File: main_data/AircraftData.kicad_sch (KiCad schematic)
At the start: 54 parts, among them J1 Orientation, J10 Shaft, J11 Wind Speed, J12 DHT, J13 RPi, J14 USB_C_Receptacle_USB2.0, J15 Control Board, J2 PROG, J3 SPI VIDEO, J4 Barometer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

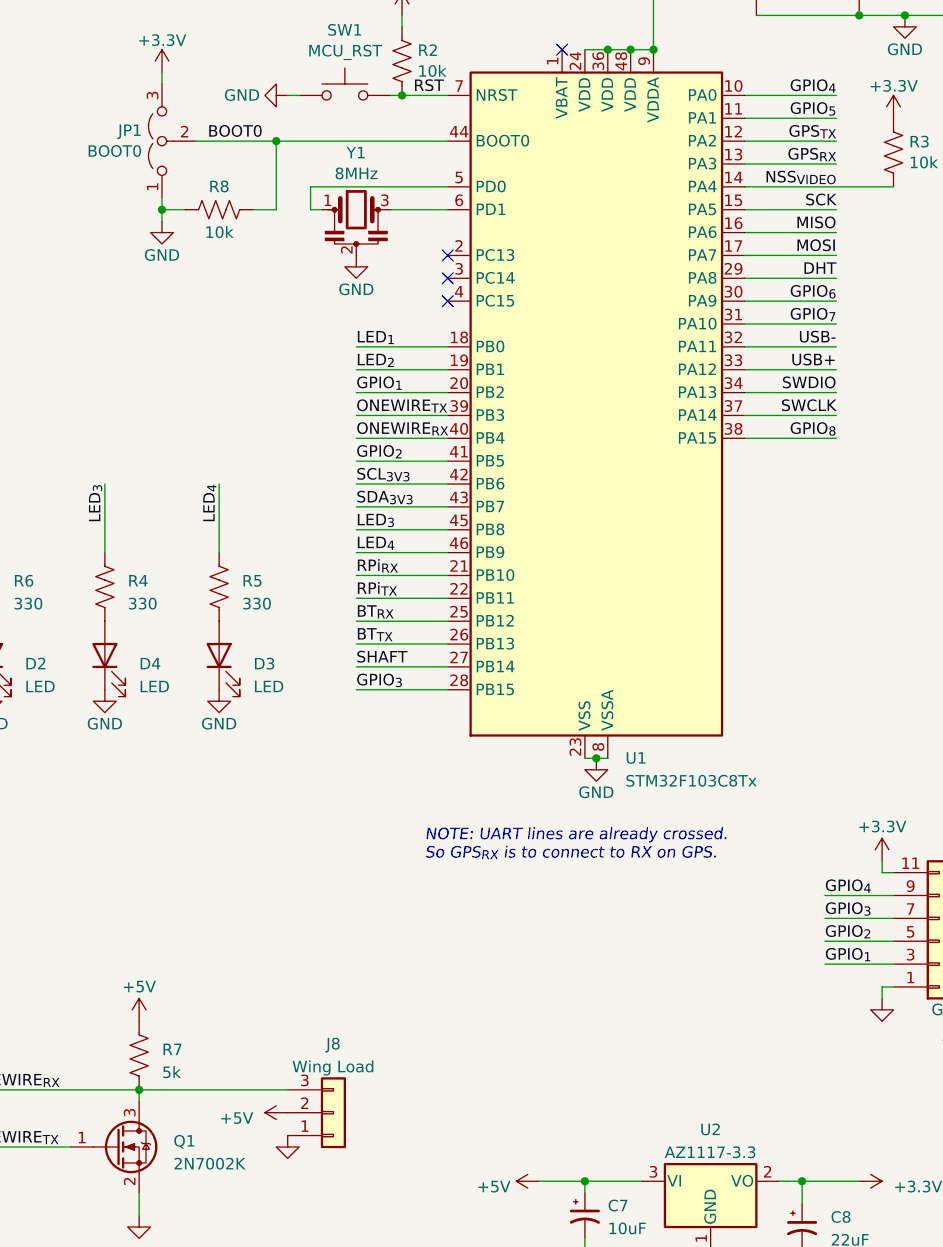
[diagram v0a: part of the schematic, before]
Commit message: Upgraded STM32
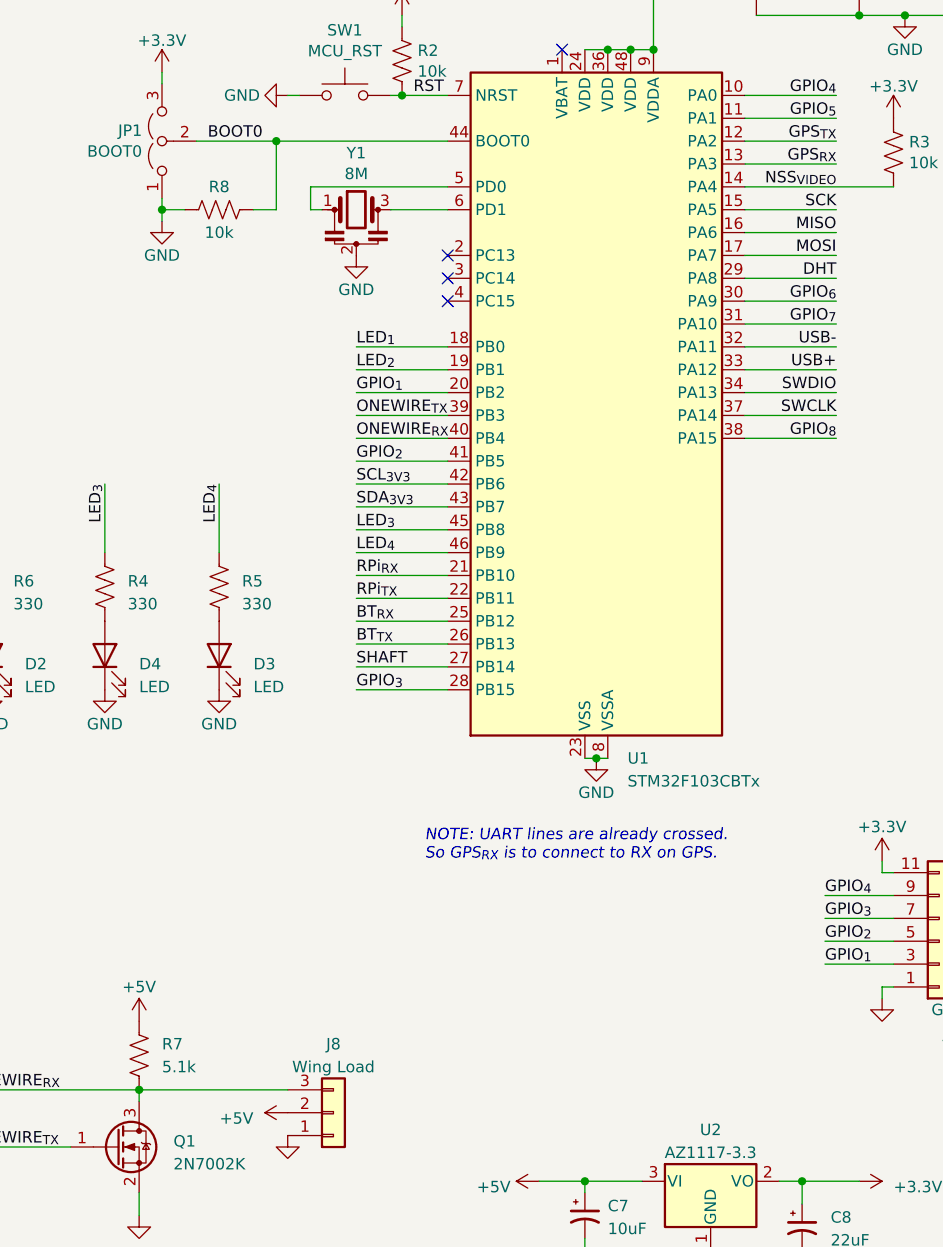
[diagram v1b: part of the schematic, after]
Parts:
- H1, H2, H3, JP1: now left out of the parts list
- R7: value 5k -> 5.1k
- U1: value STM32F103C8Tx -> STM32F103CBTx; symbol MCU_ST_STM32F1:STM32F103C8Tx -> MCU_ST_STM32F1:STM32F103CBTx
- Y1: value 8MHz -> 8M
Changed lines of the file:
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@@
   (symbol (lib_id "Device:R_US") (at 45.72 168.91 0) (unit 1)
     (in_bom yes) (on_board yes) (dnp no) (fields_autoplaced)
-    (property "Reference" "R7" (at 48.26 168.275 0)
-      (effects (font (size 1.27 1.27)) (justify left))
-    )
-    (property "Value" "5k" (at 48.26 170.815 0)
+    (property "Reference" "R7" (at 48.26 167.64 0)
+      (effects (font (size 1.27 1.27)) (justify left))
+    )
+    (property "Value" "5.1k" (at 48.26 170.18 0)
       (effects (font (size 1.27 1.27)) (justify left))
     )
@@
       (effects (font (size 1.27 1.27)))
     )
-    (property "Value" "8MHz" (at 69.85 70.9422 0)
+    (property "Value" "8M" (at 69.85 70.9422 0)
       (effects (font (size 1.27 1.27)))
     )
@@
   )
   (symbol (lib_id "Mechanical:MountingHole") (at 289.56 143.51 0) (unit 1)
-    (in_bom yes) (on_board yes) (dnp no) (fields_autoplaced)
+    (in_bom no) (on_board yes) (dnp no) (fields_autoplaced)
     (property "Reference" "H2" (at 292.1 142.875 0)
       (effects (font (size 1.27 1.27)) (justify left))
@@
     )
   )
-  (symbol (lib_id "MCU_ST_STM32F1:STM32F103C8Tx") (at 95.25 97.79 0) (unit 1)
-    (in_bom yes) (on_board yes) (dnp no) (fields_autoplaced)
-    (property "Reference" "U1" (at 99.7459 135.89 0)
-      (effects (font (size 1.27 1.27)) (justify left))
-    )
-    (property "Value" "STM32F103C8Tx" (at 99.7459 138.43 0)
+  (symbol (lib_id "MCU_ST_STM32F1:STM32F103CBTx") (at 95.25 97.79 0) (unit 1)
+    (in_bom yes) (on_board yes) (dnp no) (fields_autoplaced)
+    (property "Reference" "U1" (at 99.9841 135.89 0)
+      (effects (font (size 1.27 1.27)) (justify left))
+    )
+    (property "Value" "STM32F103CBTx" (at 99.9841 138.43 0)
       (effects (font (size 1.27 1.27)) (justify left))
     )
@@
       (effects (font (size 1.27 1.27)) (justify right) hide)
     )
-    (property "Datasheet" "https://www.st.com/resource/en/datasheet/stm32f103c8.pdf" (at 95.25 97.79 0)
+    (property "Datasheet" "https://www.st.com/resource/en/datasheet/stm32f103cb.pdf" (at 95.25 97.79 0)
       (effects (font (size 1.27 1.27)) hide)
     )
@@
   )
   (symbol (lib_id "Mechanical:MountingHole") (at 289.56 137.16 0) (unit 1)
-    (in_bom yes) (on_board yes) (dnp no) (fields_autoplaced)
+    (in_bom no) (on_board yes) (dnp no) (fields_autoplaced)
     (property "Reference" "H1" (at 292.1 136.525 0)
       (effects (font (size 1.27 1.27)) (justify left))
@@
   )
   (symbol (lib_id "Jumper:Jumper_3_Open") (at 48.26 67.31 90) (unit 1)
-    (in_bom yes) (on_board yes) (dnp no)
+    (in_bom no) (on_board yes) (dnp no)
     (property "Reference" "JP1" (at 46.0502 66.1416 90)
       (effects (font (size 1.27 1.27)) (justify left))
@@
   )
   (symbol (lib_id "Mechanical:MountingHole") (at 289.56 149.86 0) (unit 1)
-    (in_bom yes) (on_board yes) (dnp no) (fields_autoplaced)
+    (in_bom no) (on_board yes) (dnp no) (fields_autoplaced)
     (property "Reference" "H3" (at 292.1 149.225 0)
       (effects (font (size 1.27 1.27)) (justify left))
